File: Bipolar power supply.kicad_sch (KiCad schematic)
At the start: 37 parts, among them J1 Screw 6-32, J2 Screw 6-32, J3 Screw 6-32, J4 Conn_01x03, U1 LM317_TO-220, U2 LM337_TO-220

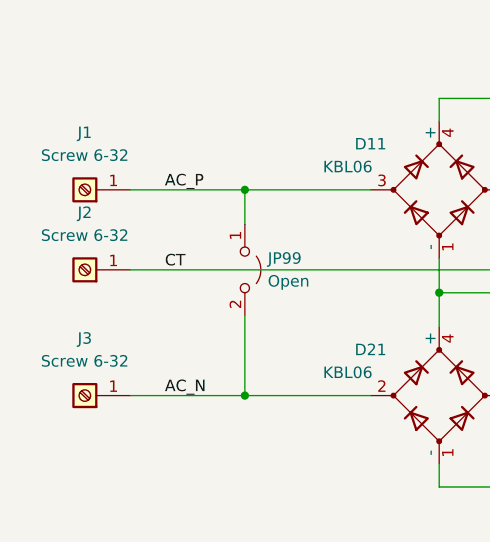
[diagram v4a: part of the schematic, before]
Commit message: Updated footprints from dry fit.
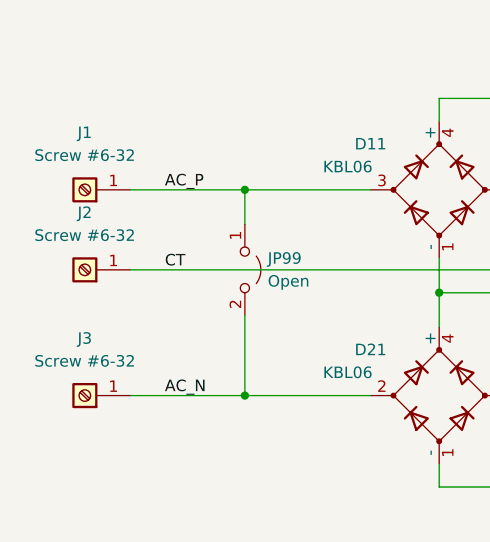
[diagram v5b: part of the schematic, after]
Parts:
- H1, H2, H3, H4: footprint MountingHole:MountingHole_3.5mm_Pad -> $Local:MountingHole_#6-32_Pad_10mm
- J1, J2, J3: value Screw 6-32 -> Screw #6-32; footprint $Local:ScrewTerminal_01x01_6-32_10mm -> $Local:ScrewTerminal_01x01_#6-32_10mm
- R15, R16, R17, R25, R26, R27: footprint Resistor_THT:R_Axial_DIN0614_L14.3mm_D5.7mm_P15.24mm_Horizontal -> $Local:R_Axial_L13.1mm_D5.6mm_P20.0mm_Horizontal
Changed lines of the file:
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@@
     (property "Reference" "R25" (id 0) (at 88.9 81.28 90))
     (property "Value" "5" (id 1) (at 88.9 83.82 90))
-    (property "Footprint" "Resistor_THT:R_Axial_DIN0614_L14.3mm_D5.7mm_P15.24mm_Horizontal" (id 2) (at 89.154 86.614 90)
+    (property "Footprint" "$Local:R_Axial_L13.1mm_D5.6mm_P20.0mm_Horizontal" (id 2) (at 89.154 86.614 90)
       (effects (font (size 1.27 1.27)) hide)
     )
@@
     (property "Reference" "R17" (id 0) (at 106.68 38.1 90))
     (property "Value" "5" (id 1) (at 106.68 40.64 90))
-    (property "Footprint" "Resistor_THT:R_Axial_DIN0614_L14.3mm_D5.7mm_P15.24mm_Horizontal" (id 2) (at 106.934 43.434 90)
+    (property "Footprint" "$Local:R_Axial_L13.1mm_D5.6mm_P20.0mm_Horizontal" (id 2) (at 106.934 43.434 90)
       (effects (font (size 1.27 1.27)) hide)
     )
@@
       (effects (font (size 1.27 1.27)) (justify left))
     )
-    (property "Footprint" "MountingHole:MountingHole_3.5mm_Pad" (id 2) (at 147.32 120.65 0)
+    (property "Footprint" "$Local:MountingHole_#6-32_Pad_10mm" (id 2) (at 147.32 120.65 0)
       (effects (font (size 1.27 1.27)) hide)
     )
@@
     (property "Reference" "R15" (id 0) (at 88.9 38.1 90))
     (property "Value" "5" (id 1) (at 88.9 40.64 90))
-    (property "Footprint" "Resistor_THT:R_Axial_DIN0614_L14.3mm_D5.7mm_P15.24mm_Horizontal" (id 2) (at 89.154 43.434 90)
+    (property "Footprint" "$Local:R_Axial_L13.1mm_D5.6mm_P20.0mm_Horizontal" (id 2) (at 89.154 43.434 90)
       (effects (font (size 1.27 1.27)) hide)
     )
@@
     (in_bom yes) (on_board yes) (fields_autoplaced)
     (property "Reference" "J1" (id 0) (at 35.56 48.26 0))
-    (property "Value" "Screw 6-32" (id 1) (at 35.56 50.8 0))
-    (property "Footprint" "$Local:ScrewTerminal_01x01_6-32_10mm" (id 2) (at 35.56 54.61 0)
+    (property "Value" "Screw #6-32" (id 1) (at 35.56 50.8 0))
+    (property "Footprint" "$Local:ScrewTerminal_01x01_#6-32_10mm" (id 2) (at 35.56 54.61 0)
       (effects (font (size 1.27 1.27)) hide)
     )
@@
     (property "Reference" "R27" (id 0) (at 106.68 81.28 90))
     (property "Value" "5" (id 1) (at 106.68 83.82 90))
-    (property "Footprint" "Resistor_THT:R_Axial_DIN0614_L14.3mm_D5.7mm_P15.24mm_Horizontal" (id 2) (at 106.934 86.614 90)
+    (property "Footprint" "$Local:R_Axial_L13.1mm_D5.6mm_P20.0mm_Horizontal" (id 2) (at 106.934 86.614 90)
       (effects (font (size 1.27 1.27)) hide)
     )
@@
     (in_bom yes) (on_board yes) (fields_autoplaced)
     (property "Reference" "J2" (id 0) (at 35.56 57.15 0))
-    (property "Value" "Screw 6-32" (id 1) (at 35.56 59.69 0))
-    (property "Footprint" "$Local:ScrewTerminal_01x01_6-32_10mm" (id 2) (at 35.56 63.5 0)
+    (property "Value" "Screw #6-32" (id 1) (at 35.56 59.69 0))
+    (property "Footprint" "$Local:ScrewTerminal_01x01_#6-32_10mm" (id 2) (at 35.56 63.5 0)
       (effects (font (size 1.27 1.27)) hide)
     )
@@
       (effects (font (size 1.27 1.27)) (justify left))
     )
-    (property "Footprint" "MountingHole:MountingHole_3.5mm_Pad" (id 2) (at 125.73 128.27 0)
+    (property "Footprint" "$Local:MountingHole_#6-32_Pad_10mm" (id 2) (at 125.73 128.27 0)
       (effects (font (size 1.27 1.27)) hide)
     )
@@
       (effects (font (size 1.27 1.27)) (justify left))
     )
-    (property "Footprint" "MountingHole:MountingHole_3.5mm_Pad" (id 2) (at 125.73 120.65 0)
+    (property "Footprint" "$Local:MountingHole_#6-32_Pad_10mm" (id 2) (at 125.73 120.65 0)
       (effects (font (size 1.27 1.27)) hide)
     )
@@
     (property "Reference" "R16" (id 0) (at 97.79 38.1 90))
     (property "Value" "5" (id 1) (at 97.79 40.64 90))
-    (property "Footprint" "Resistor_THT:R_Axial_DIN0614_L14.3mm_D5.7mm_P15.24mm_Horizontal" (id 2) (at 98.044 43.434 90)
+    (property "Footprint" "$Local:R_Axial_L13.1mm_D5.6mm_P20.0mm_Horizontal" (id 2) (at 98.044 43.434 90)
       (effects (font (size 1.27 1.27)) hide)
     )
@@
       (effects (font (size 1.27 1.27)) (justify left))
     )
-    (property "Footprint" "MountingHole:MountingHole_3.5mm_Pad" (id 2) (at 147.32 128.27 0)
+    (property "Footprint" "$Local:MountingHole_#6-32_Pad_10mm" (id 2) (at 147.32 128.27 0)
       (effects (font (size 1.27 1.27)) hide)
     )
@@
     (property "Reference" "R26" (id 0) (at 97.79 81.28 90))
     (property "Value" "5" (id 1) (at 97.79 83.82 90))
-    (property "Footprint" "Resistor_THT:R_Axial_DIN0614_L14.3mm_D5.7mm_P15.24mm_Horizontal" (id 2) (at 98.044 86.614 90)
+    (property "Footprint" "$Local:R_Axial_L13.1mm_D5.6mm_P20.0mm_Horizontal" (id 2) (at 98.044 86.614 90)
       (effects (font (size 1.27 1.27)) hide)
     )
@@
     (in_bom yes) (on_board yes) (fields_autoplaced)
     (property "Reference" "J3" (id 0) (at 35.56 71.12 0))
-    (property "Value" "Screw 6-32" (id 1) (at 35.56 73.66 0))
-    (property "Footprint" "$Local:ScrewTerminal_01x01_6-32_10mm" (id 2) (at 35.56 77.47 0)
+    (property "Value" "Screw #6-32" (id 1) (at 35.56 73.66 0))
+    (property "Footprint" "$Local:ScrewTerminal_01x01_#6-32_10mm" (id 2) (at 35.56 77.47 0)
       (effects (font (size 1.27 1.27)) hide)
     )
@@
     )
     (path "/b11a1dad-6250-4ef9-a0d5-2cdacc2ad47f"
-      (reference "H1") (unit 1) (value "MountingHole") (footprint "MountingHole:MountingHole_3.5mm_Pad")
+      (reference "H1") (unit 1) (value "MountingHole") (footprint "$Local:MountingHole_#6-32_Pad_10mm")
     )
     (path "/a3fbb6b3-491c-4daf-be3b-e03a3fd2ac24"
-      (reference "H2") (unit 1) (value "MountingHole") (footprint "MountingHole:MountingHole_3.5mm_Pad")
+      (reference "H2") (unit 1) (value "MountingHole") (footprint "$Local:MountingHole_#6-32_Pad_10mm")
     )
     (path "/52140783-2370-49be-abec-a1ff28f5dd80"
-      (reference "H3") (unit 1) (value "MountingHole") (footprint "MountingHole:MountingHole_3.5mm_Pad")
+      (reference "H3") (unit 1) (value "MountingHole") (footprint "$Local:MountingHole_#6-32_Pad_10mm")
     )
     (path "/db3fc07e-8c67-42ff-8405-b71dbb17507d"
-      (reference "H4") (unit 1) (value "MountingHole") (footprint "MountingHole:MountingHole_3.5mm_Pad")
+      (reference "H4") (unit 1) (value "MountingHole") (footprint "$Local:MountingHole_#6-32_Pad_10mm")
     )
     (path "/535d75f3-a892-4abf-8df5-b9b3a0a52e38"
-      (reference "J1") (unit 1) (value "Screw 6-32") (footprint "$Local:ScrewTerminal_01x01_6-32_10mm")
+      (reference "J1") (unit 1) (value "Screw #6-32") (footprint "$Local:ScrewTerminal_01x01_#6-32_10mm")
     )
     (path "/9af01e5e-b55c-458f-aacd-833e3b134134"
-      (reference "J2") (unit 1) (value "Screw 6-32") (footprint "$Local:ScrewTerminal_01x01_6-32_10mm")
+      (reference "J2") (unit 1) (value "Screw #6-32") (footprint "$Local:ScrewTerminal_01x01_#6-32_10mm")
     )
     (path "/f475557a-9db8-434a-90c5-c18389084737"
-      (reference "J3") (unit 1) (value "Screw 6-32") (footprint "$Local:ScrewTerminal_01x01_6-32_10mm")
+      (reference "J3") (unit 1) (value "Screw #6-32") (footprint "$Local:ScrewTerminal_01x01_#6-32_10mm")
     )
     (path "/1e911689-f270-41bf-8e59-4bf5fee84976"
@@
     )
     (path "/5273bb82-bb5d-4a20-9cd2-d8406d1af85b"
-      (reference "R15") (unit 1) (value "5") (footprint "Resistor_THT:R_Axial_DIN0614_L14.3mm_D5.7mm_P15.24mm_Horizontal")
+      (reference "R15") (unit 1) (value "5") (footprint "$Local:R_Axial_L13.1mm_D5.6mm_P20.0mm_Horizontal")
     )
     (path "/d88546dd-5c42-4bc0-a89d-ecef39806a20"
-      (reference "R16") (unit 1) (value "5") (footprint "Resistor_THT:R_Axial_DIN0614_L14.3mm_D5.7mm_P15.24mm_Horizontal")
+      (reference "R16") (unit 1) (value "5") (footprint "$Local:R_Axial_L13.1mm_D5.6mm_P20.0mm_Horizontal")
     )
     (path "/361902c0-544b-4455-a119-6555914a3004"
-      (reference "R17") (unit 1) (value "5") (footprint "Resistor_THT:R_Axial_DIN0614_L14.3mm_D5.7mm_P15.24mm_Horizontal")
+      (reference "R17") (unit 1) (value "5") (footprint "$Local:R_Axial_L13.1mm_D5.6mm_P20.0mm_Horizontal")
     )
     (path "/eaec5175-ff90-44b5-8e28-844a21070a0d"
@@
     )
     (path "/2701913f-0fae-4973-949e-b79d2c88eb7f"
-      (reference "R25") (unit 1) (value "5") (footprint "Resistor_THT:R_Axial_DIN0614_L14.3mm_D5.7mm_P15.24mm_Horizontal")
+      (reference "R25") (unit 1) (value "5") (footprint "$Local:R_Axial_L13.1mm_D5.6mm_P20.0mm_Horizontal")
     )
     (path "/e4fe2eb6-b68b-4512-a711-7ceebaa23555"
-      (reference "R26") (unit 1) (value "5") (footprint "Resistor_THT:R_Axial_DIN0614_L14.3mm_D5.7mm_P15.24mm_Horizontal")
+      (reference "R26") (unit 1) (value "5") (footprint "$Local:R_Axial_L13.1mm_D5.6mm_P20.0mm_Horizontal")
     )
     (path "/8fad684b-7593-4e43-9c97-180d84a4716d"
-      (reference "R27") (unit 1) (value "5") (footprint "Resistor_THT:R_Axial_DIN0614_L14.3mm_D5.7mm_P15.24mm_Horizontal")
+      (reference "R27") (unit 1) (value "5") (footprint "$Local:R_Axial_L13.1mm_D5.6mm_P20.0mm_Horizontal")
     )
     (path "/dfa102b1-17da-44f4-a9e1-ead862583975"

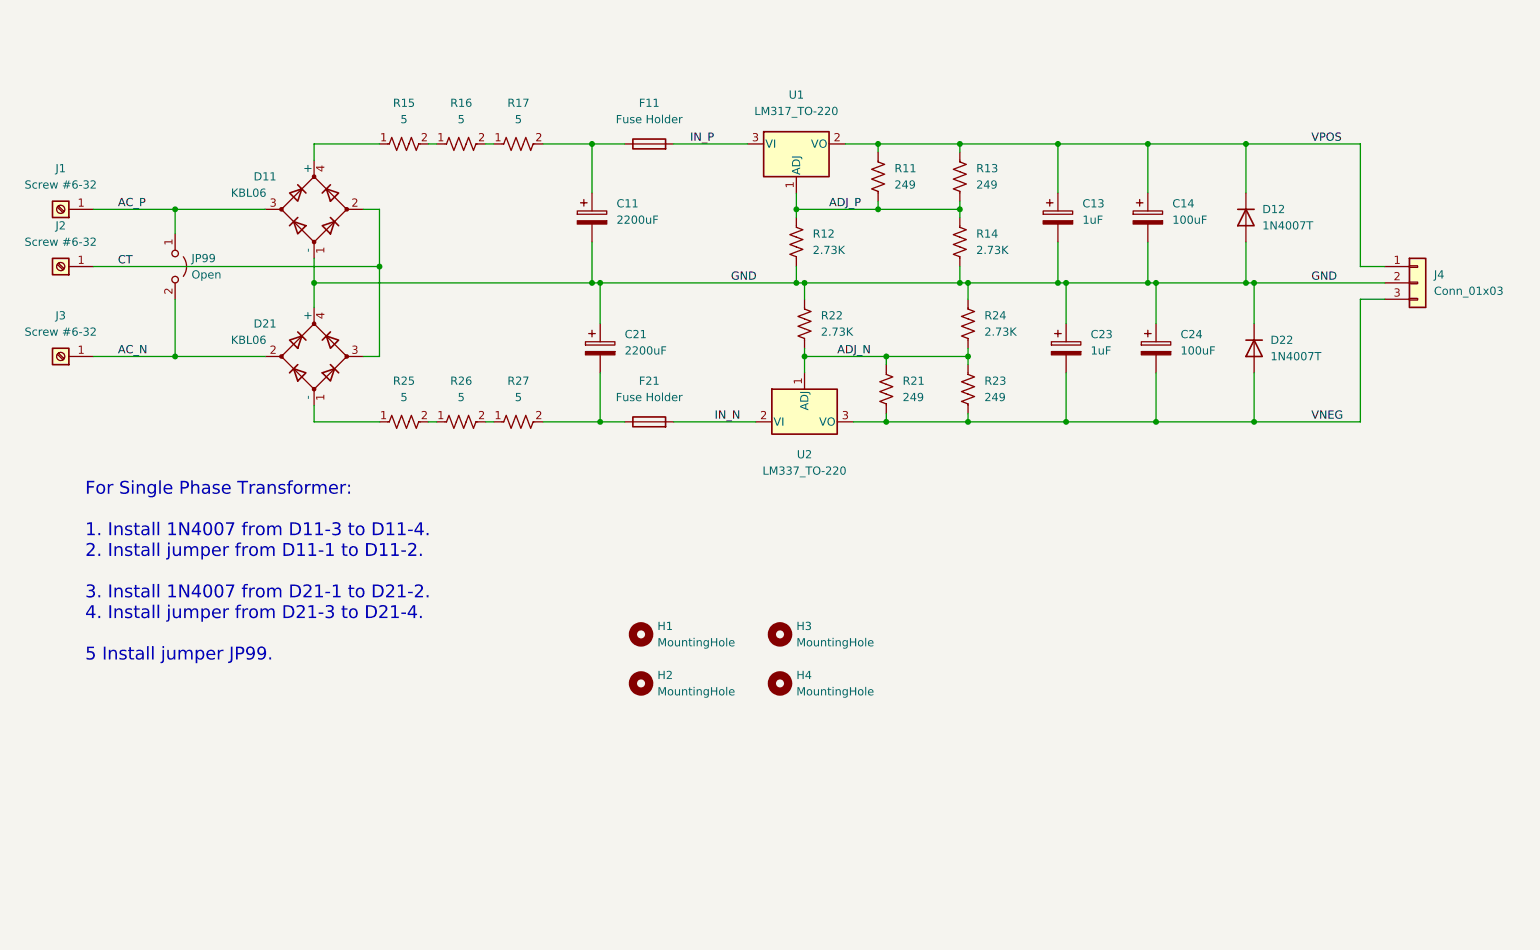
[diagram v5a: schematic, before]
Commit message: Added LEDs and edge clearance. Rerouted.
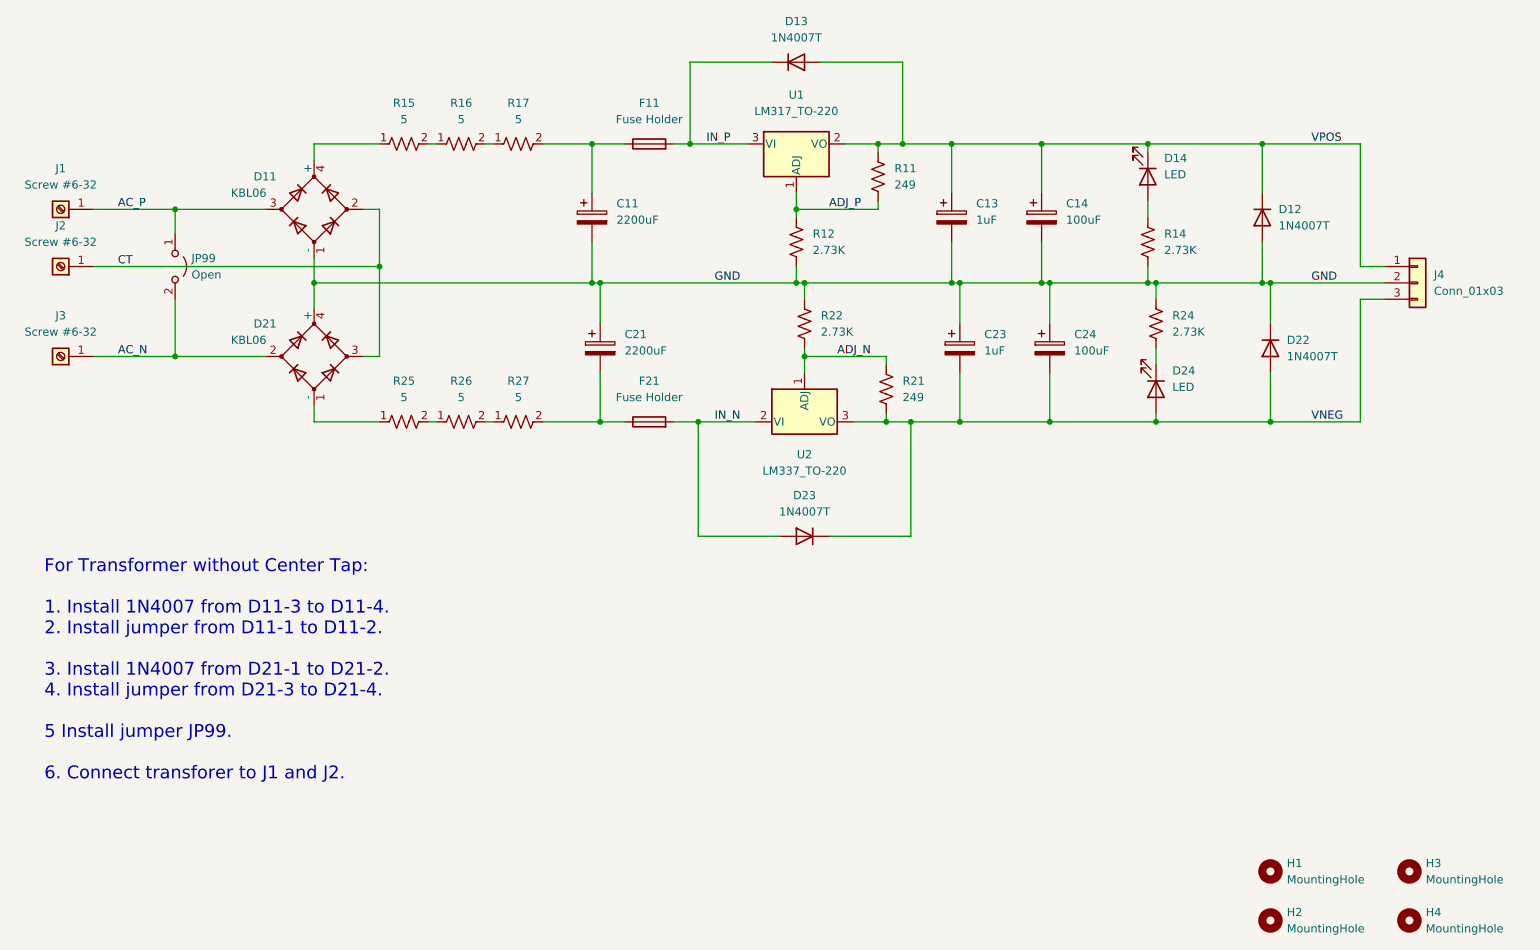
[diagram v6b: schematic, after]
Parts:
- removed R13, R23: 249, $Local:R_0805_2012Metric_Pad1.20x1.40mm_HandSolder, symbol Device:R_US
- added D13, D23: 1N4007T, Diode_THT:D_DO-41_SOD81_P10.16mm_Horizontal, symbol Device:D
- added D14, D24: LED, $Local:LED_D5.0mm, symbol Device:LED
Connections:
- net ADJ_N: no longer R24.2
- net ADJ_P: no longer R14.1
- net IN_N: now also D23.2 (A)
- net IN_P: now also D13.1 (K)
- net VNEG: now also D23.1 (K), D24.2 (A)
- net VPOS: now also D13.2 (A), D14.1 (K)
- new net: D24.1 (K), R24.2
- new net: D14.2 (A), R14.1
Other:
- note added: "For Transformer without Center Tap: 1. Install 1N4007 from D11-3 to D11-4. 2. Install jumper from D11-1 to D11-2. 3. Install 1N4007 from D21-1 to D21-2. 4. Install jumper from D21-3 to D21-4. 5 Install jumper JP99. 6. Connect transforer to J1 and J2."
- note removed: "For Single Phase Transformer: 1. Install 1N4007 from D11-3 to D11-4. 2. Install jumper from D11-1 to D11-2. 3. Install 1N4007 from D21-1 to D21-2. 4. Install jumper from D21-3 to D21-4. 5 Install jumper JP99."
- moved on the sheet: C13, C14, C23, C24, D12, D22, H1, H2, H3, H4, R14, R24

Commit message: Switched to non-CT transformer. Redesigned and rerouted.
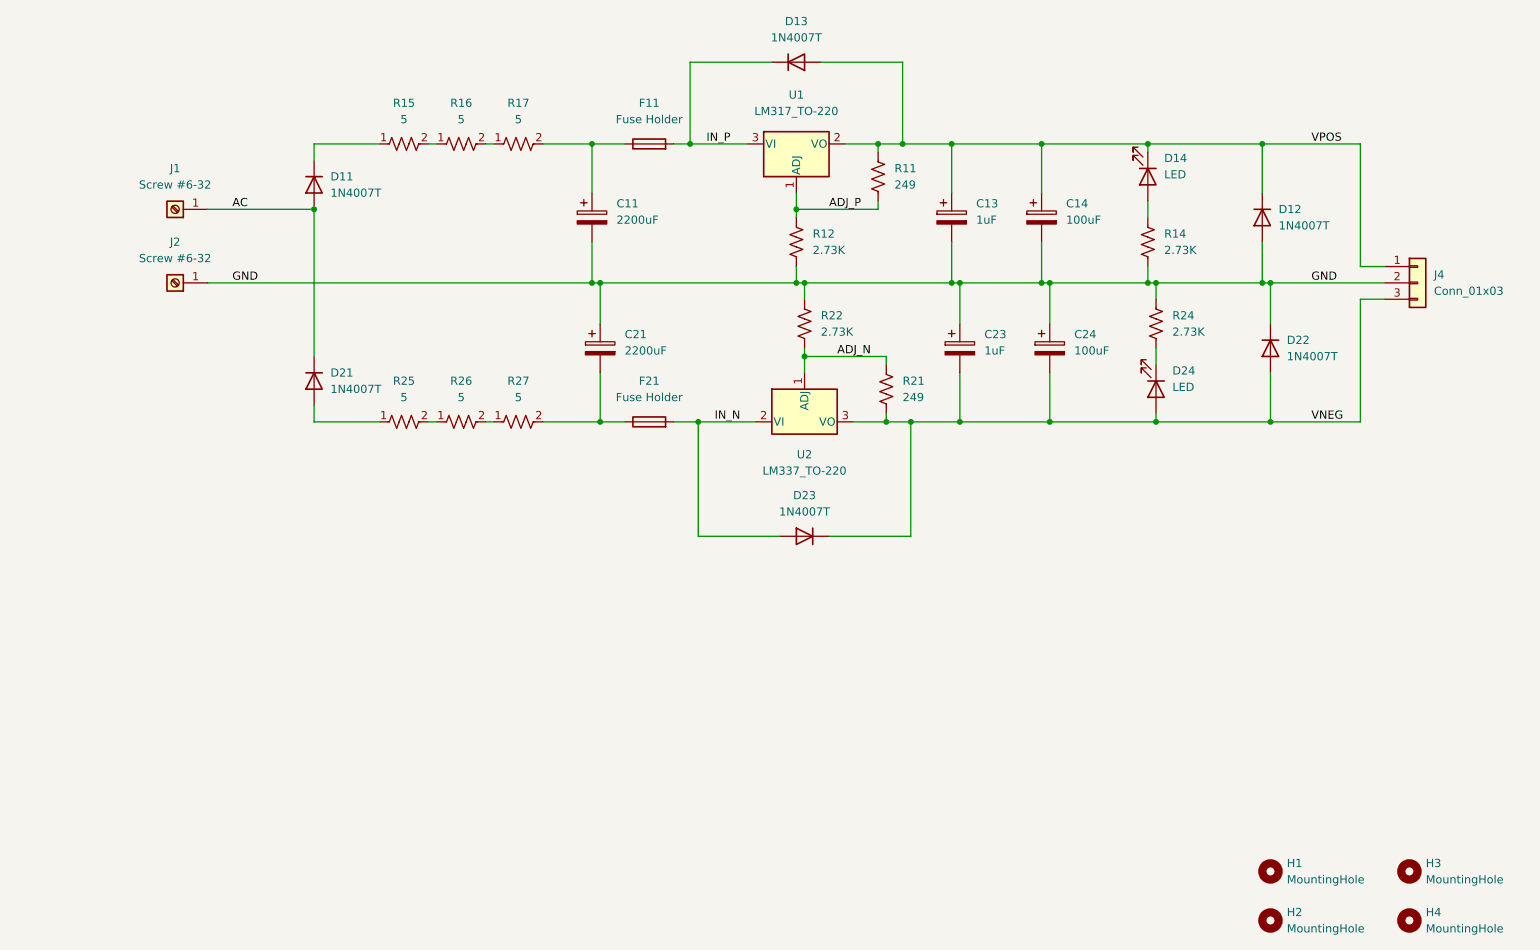
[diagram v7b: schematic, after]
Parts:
- removed D11, D21: KBL06, Diode_THT:Diode_Bridge_Vishay_KBL, symbol Device:D_Bridge_-AA+
- removed J3: Screw #6-32, $Local:ScrewTerminal_01x01_#6-32_10mm, symbol Connector:Screw_Terminal_01x01
- removed JP99: Open, $Local:Jumper_P25.40mm, symbol Jumper:Jumper_2_Open
- added D11, D21: 1N4007T, Diode_THT:D_DO-41_SOD81_P10.16mm_Horizontal, symbol Device:D
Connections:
- net CT is gone; now on net GND: J2.1 (Pin_1)
- net at R25.1: now also D21.2 (A)
- net at R15.1: now also D11.1 (K)
- net AC_P renamed AC
- net AC: now also D11.2 (A), D21.1 (K)
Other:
- note removed: "For Transformer without Center Tap: 1. Install 1N4007 from D11-3 to D11-4. 2. Install jumper from D11-1 to D11-2. 3. Install 1N4007 from D21-1 to D21-2. 4. Install jumper from D21-3 to D21-4. 5 Install jumper JP99. 6. Connect transforer to J1 and J2."
- moved on the sheet: J1, J2
